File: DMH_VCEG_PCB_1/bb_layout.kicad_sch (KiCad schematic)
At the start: 0 parts

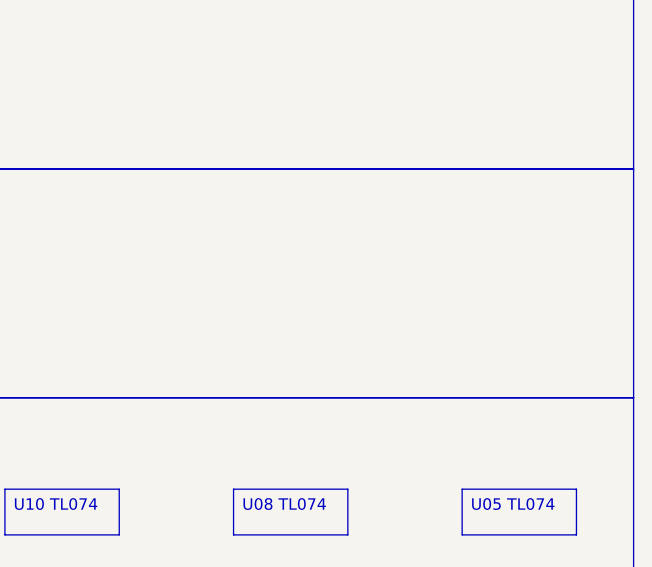
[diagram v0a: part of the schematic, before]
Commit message: Small changes during breadboarding
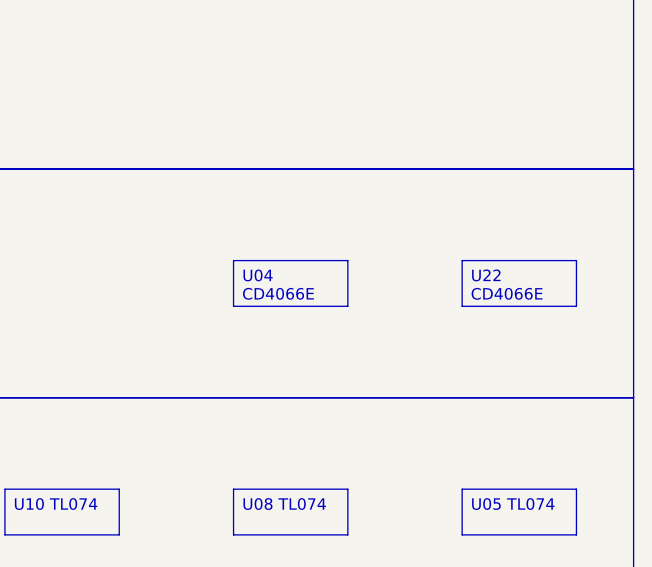
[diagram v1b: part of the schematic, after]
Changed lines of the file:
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@@
+		)
+	)
+	(text_box "U22 CD4066E"
+		(exclude_from_sim no)
+		(at 133.35 86.36 0)
+		(size 12.7 5.08)
+		(margins 0.9525 0.9525 0.9525 0.9525)
+		(stroke
+			(width 0)
+			(type solid)
+		)
+		(fill
+			(type none)
+		)
+		(effects
+			(font
+				(size 1.27 1.27)
+			)
+			(justify left top)
 		)
 	)
@@
 		(size 12.7 5.08)
 		(margins 0.9525 0.9525 0.9525 0.9525)
+		(stroke
+			(width 0)
+			(type solid)
+		)
+		(fill
+			(type none)
+		)
+		(effects
+			(font
+				(size 1.27 1.27)
+			)
+			(justify left top)
+		)
+	)
+	(text_box "U04 CD4066E"
+		(exclude_from_sim no)
+		(at 107.95 86.36 0)
+		(size 12.7 5.08)
+		(margins 0.9525 0.9525 0.9525 0.9525)

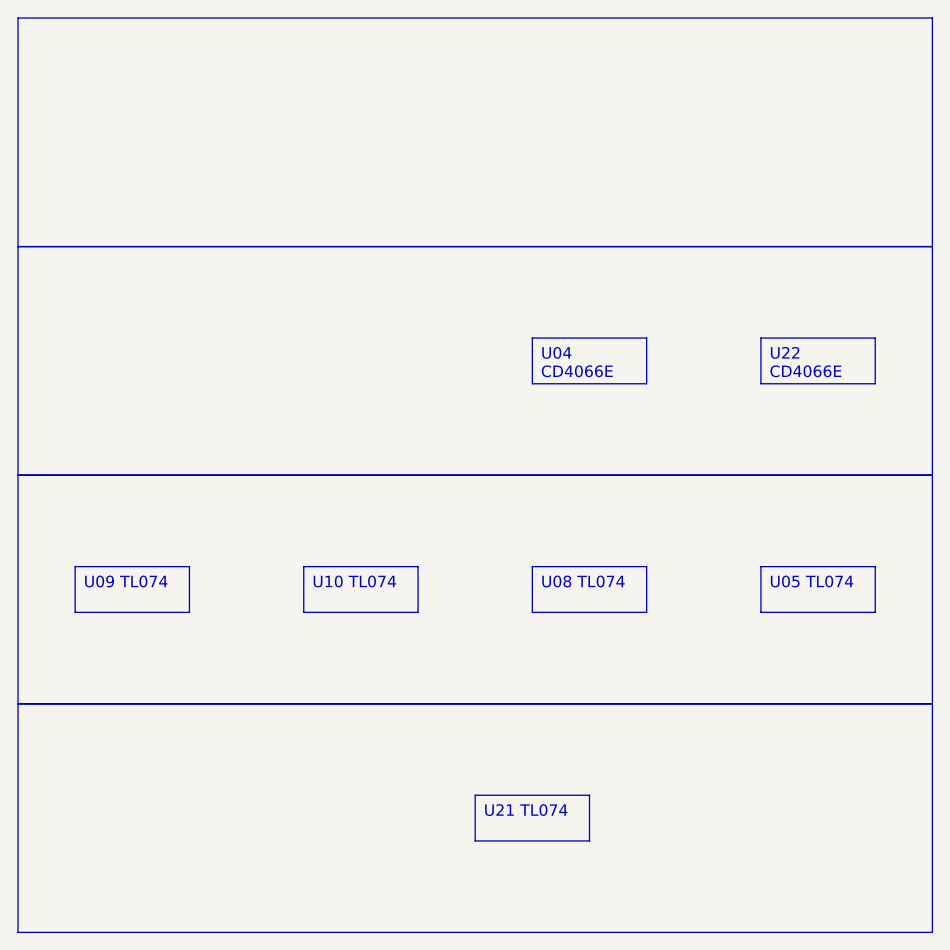
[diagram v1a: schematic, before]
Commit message: Mods on PCB 1 after breadboarding
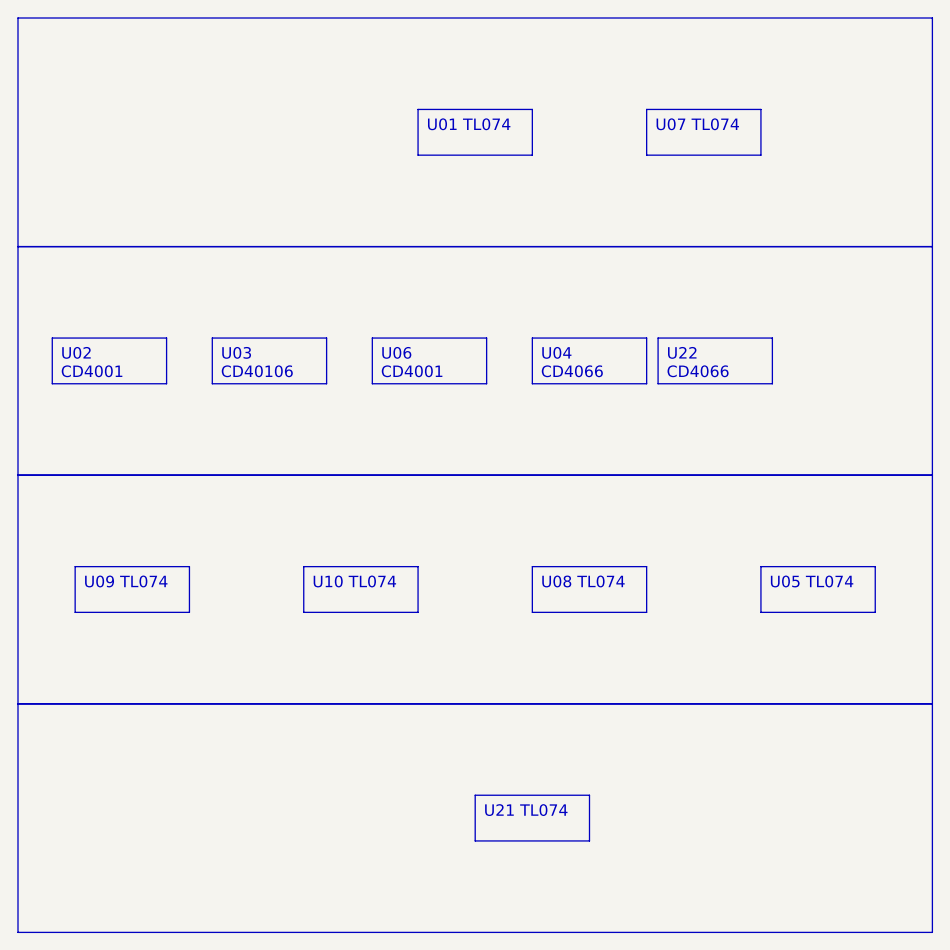
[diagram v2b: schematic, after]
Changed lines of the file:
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@@
 		)
 	)
-	(text_box "U22 CD4066E"
+	(text_box "U01 TL074"
 		(exclude_from_sim no)
-		(at 133.35 86.36 0)
+		(at 95.25 60.96 0)
+		(size 12.7 5.08)
+		(margins 0.9525 0.9525 0.9525 0.9525)
+		(stroke
+			(width 0)
+			(type solid)
+		)
+		(fill
+			(type none)
+		)
+		(effects
+			(font
+				(size 1.27 1.27)
+			)
+			(justify left top)
+		)
+	)
+	(text_box "U03 CD40106"
+		(exclude_from_sim no)
+		(at 72.39 86.36 0)
+		(size 12.7 5.08)
+		(margins 0.9525 0.9525 0.9525 0.9525)
+		(stroke
+			(width 0)
+			(type solid)
+		)
+		(fill
+			(type none)
+		)
+		(effects
+			(font
+				(size 1.27 1.27)
+			)
+			(justify left top)
+		)
+	)
+	(text_box "U22 CD4066"
+		(exclude_from_sim no)
+		(at 121.92 86.36 0)
+		(size 12.7 5.08)
+		(margins 0.9525 0.9525 0.9525 0.9525)
+		(stroke
+			(width 0)
+			(type solid)
+		)
+		(fill
+			(type none)
+		)
+		(effects
+			(font
+				(size 1.27 1.27)
+			)
+			(justify left top)
+		)
+	)
+	(text_box "U07 TL074"
+		(exclude_from_sim no)
+		(at 120.65 60.96 0)
 		(size 12.7 5.08)
 		(margins 0.9525 0.9525 0.9525 0.9525)
@@
 		)
 	)
+	(text_box "U06 CD4001"
+		(exclude_from_sim no)
+		(at 90.17 86.36 0)
+		(size 12.7 5.08)
+		(margins 0.9525 0.9525 0.9525 0.9525)
+		(stroke
+			(width 0)
+			(type solid)
+		)
+		(fill
+			(type none)
+		)
+		(effects
+			(font
+				(size 1.27 1.27)
+			)
+			(justify left top)
+		)
+	)
 	(text_box "U08 TL074"
 		(exclude_from_sim no)
@@
 		)
 	)
-	(text_box "U04 CD4066E"
+	(text_box "U04 CD4066"
 		(exclude_from_sim no)
 		(at 107.95 86.36 0)
 		(size 12.7 5.08)
 		(margins 0.9525 0.9525 0.9525 0.9525)
+		(stroke
+			(width 0)
+			(type solid)
+		)
+		(fill
+			(type none)
+		)
+		(effects
+			(font
+				(size 1.27 1.27)
+			)
+			(justify left top)
+		)
+	)
+	(text_box "U02 CD4001"
+		(exclude_from_sim no)
+		(at 54.61 86.36 0)
+		(size 12.7 5.08)
+		(margins 0.9525 0.9525 0.9525 0.9525)
